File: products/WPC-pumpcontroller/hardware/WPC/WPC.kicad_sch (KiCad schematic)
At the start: 43 parts, among them J1 NoPWR_CONN, J2 Conn_Coaxial_Small, J3 PWR_CONN, J4 Conn_IN, U13 AMS1117-5.0, U5 ESP32 30 Pin CP2102 Developme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, U7 ISC-SX1262-B, U8 AP2112K-3.3

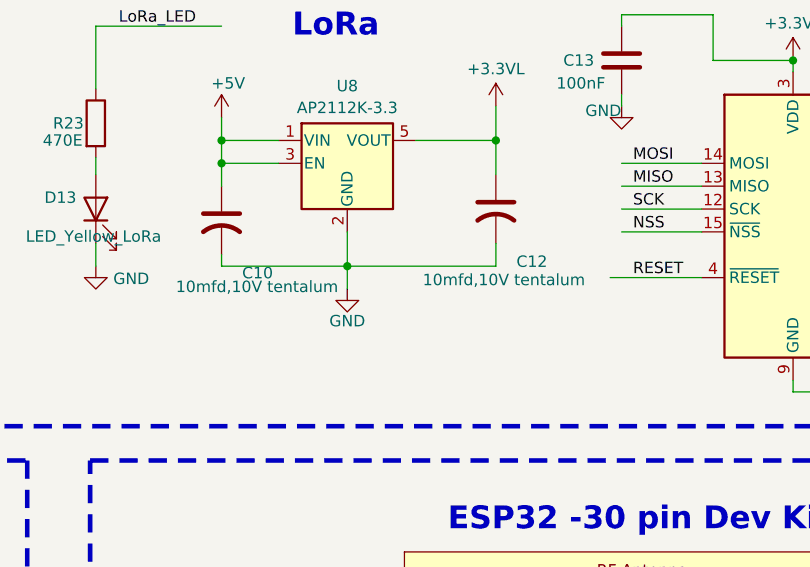
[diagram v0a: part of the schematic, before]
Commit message: WPC: PumpNode + WPC board updates, add 2x panel and Gerber exports
- Update PumpNode and WPC KiCad PCB/schematic/project-local files
- Add WPC-panel2x (2-up panelized PumpNode layout) KiCad project
- Add Gerber/drill export sets for PumpNode and the 2x panel

Co-Authored-By: Claude Sonnet 5 <noreply@anthropic.com>
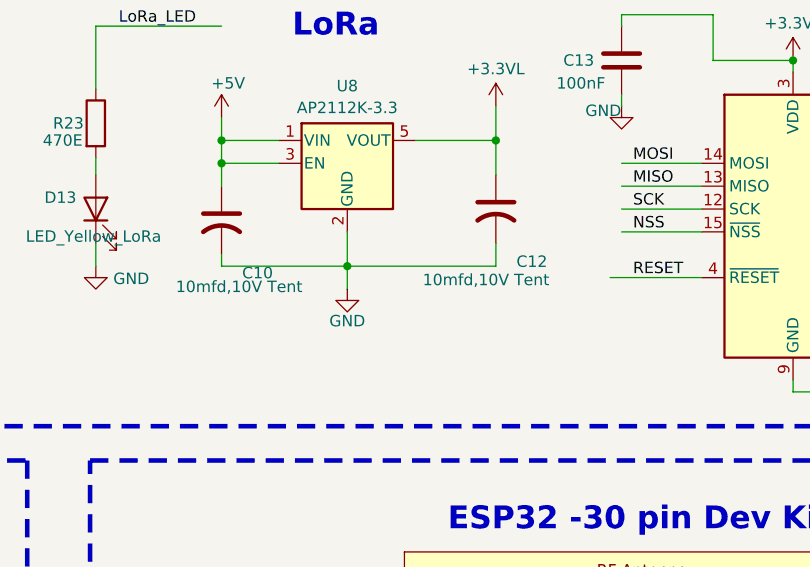
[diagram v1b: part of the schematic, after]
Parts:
- C10, C12: value 10mfd,10V tentalum -> 10mfd,10V Tent; footprint Capacitor_SMD:C_0603_1608Metric -> Capacitor_SMD:C_0805_2012Metric
- D1, D13, D2, D3, D7: footprint LED_SMD:LED_0603_1608Metric -> LED_SMD:LED_1206_3216Metric
- D4, D5, D6, D8: footprint Diode_SMD:D_SOD-882 -> Diode_SMD:D_0603_1608Metric
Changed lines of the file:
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@@
 			)
 		)
-		(property "Footprint" "LED_SMD:LED_0603_1608Metric"
+		(property "Footprint" "LED_SMD:LED_1206_3216Metric"
 			(at 204.47 200.66 0)
 			(effects
@@
 			)
 		)
-		(property "Footprint" "LED_SMD:LED_0603_1608Metric"
+		(property "Footprint" "LED_SMD:LED_1206_3216Metric"
 			(at 92.71 210.82 0)
 			(effects
@@
 			)
 		)
-		(property "Value" "10mfd,10V tentalum"
+		(property "Value" "10mfd,10V Tent"
 			(at 200.152 63.754 0)
 			(effects
@@
 			)
 		)
-		(property "Footprint" "Capacitor_SMD:C_0603_1608Metric"
+		(property "Footprint" "Capacitor_SMD:C_0805_2012Metric"
 			(at 208.28 55.88 0)
 			(effects
@@
 			)
 		)
-		(property "Value" "10mfd,10V tentalum"
+		(property "Value" "10mfd,10V Tent"
 			(at 172.72 64.516 0)
 			(effects
@@
 			)
 		)
-		(property "Footprint" "Capacitor_SMD:C_0603_1608Metric"
+		(property "Footprint" "Capacitor_SMD:C_0805_2012Metric"
 			(at 177.8 57.15 0)
 			(effects
@@
 			)
 		)
-		(property "Footprint" "LED_SMD:LED_0603_1608Metric"
+		(property "Footprint" "LED_SMD:LED_1206_3216Metric"
 			(at 163.83 55.88 0)
 			(effects
@@
 			)
 		)
-		(property "Footprint" "LED_SMD:LED_0603_1608Metric"
+		(property "Footprint" "LED_SMD:LED_1206_3216Metric"
 			(at 93.98 157.48 0)
 			(effects
@@
 			)
 		)
-		(property "Footprint" "LED_SMD:LED_0603_1608Metric"
+		(property "Footprint" "LED_SMD:LED_1206_3216Metric"
 			(at 93.98 104.14 0)
 			(effects
@@
 			)
 		)
-		(property "Footprint" "Diode_SMD:D_SOD-882"
+		(property "Footprint" "Diode_SMD:D_0603_1608Metric"
 			(at 105.41 173.99 0)
 			(effects
@@
 			)
 		)
-		(property "Footprint" "Diode_SMD:D_SOD-882"
+		(property "Footprint" "Diode_SMD:D_0603_1608Metric"
 			(at 215.9 217.17 0)
 			(effects
@@
 			)
 		)
-		(property "Footprint" "Diode_SMD:D_SOD-882"
+		(property "Footprint" "Diode_SMD:D_0603_1608Metric"
 			(at 104.14 227.33 0)
 			(effects
@@
 			)
 		)
-		(property "Footprint" "Diode_SMD:D_SOD-882"
+		(property "Footprint" "Diode_SMD:D_0603_1608Metric"
 			(at 105.41 120.65 0)
 			(effects
